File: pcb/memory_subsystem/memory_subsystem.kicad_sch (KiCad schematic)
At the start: 0 parts

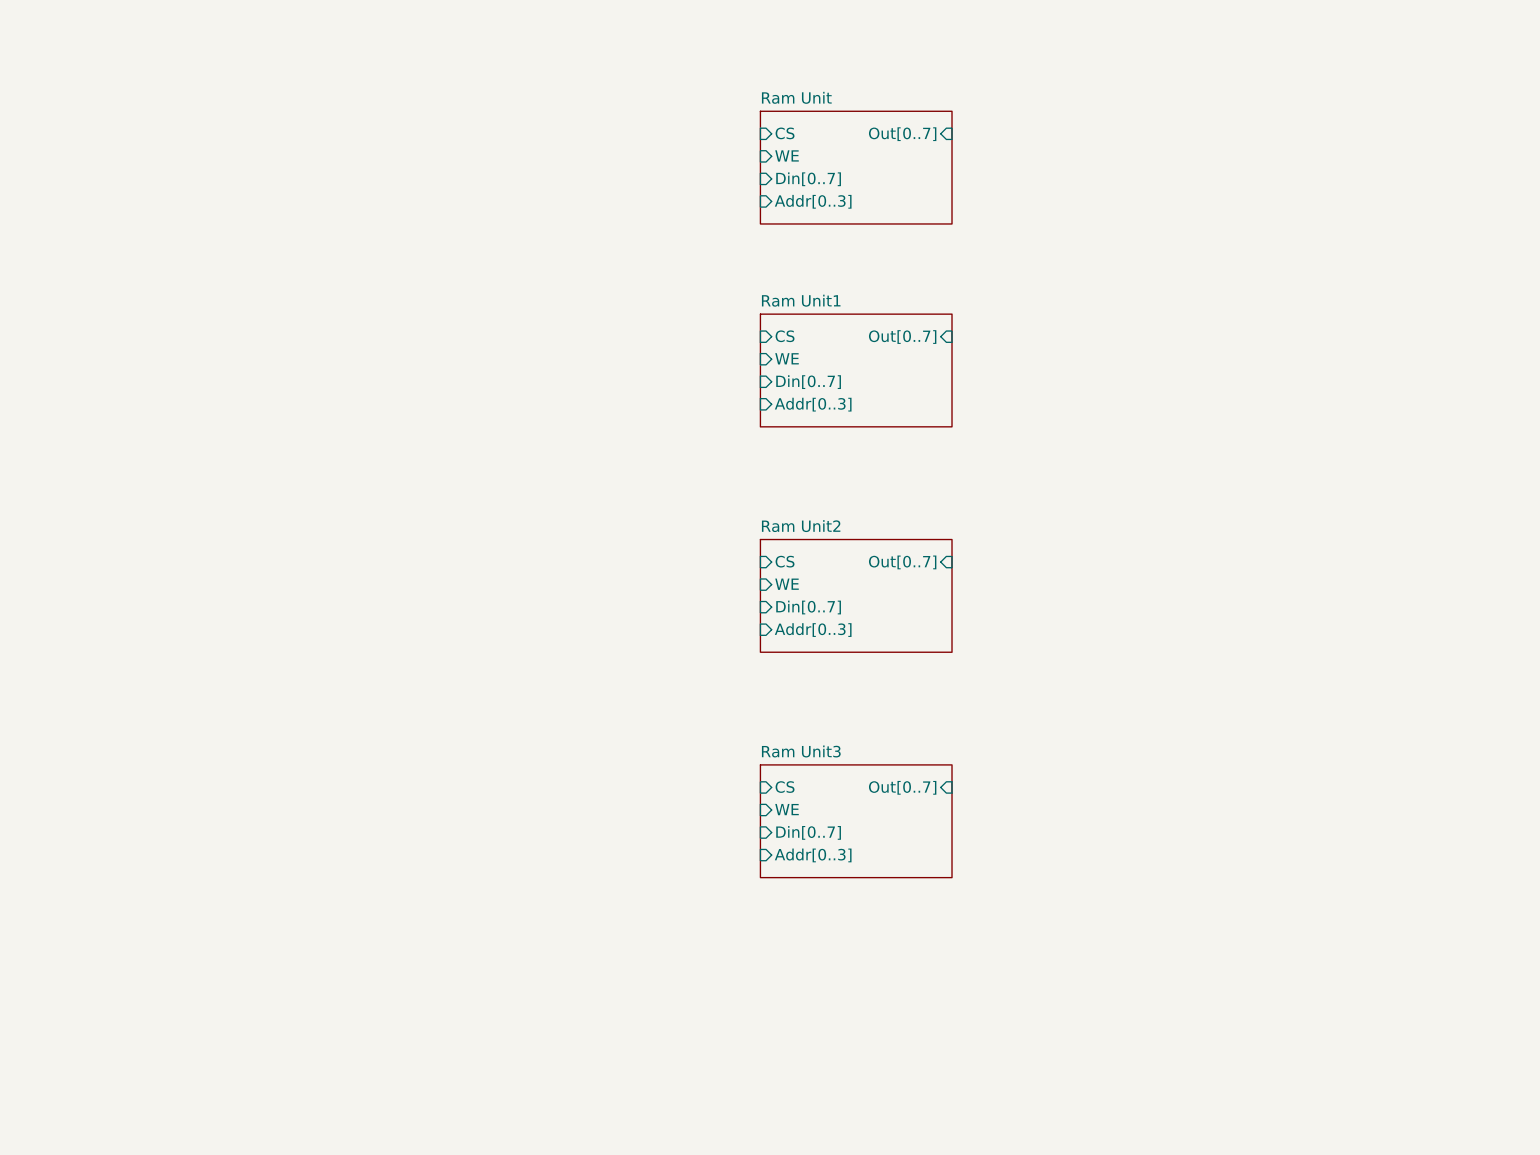
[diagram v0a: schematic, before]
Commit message: Finished first draft of memory subsystem
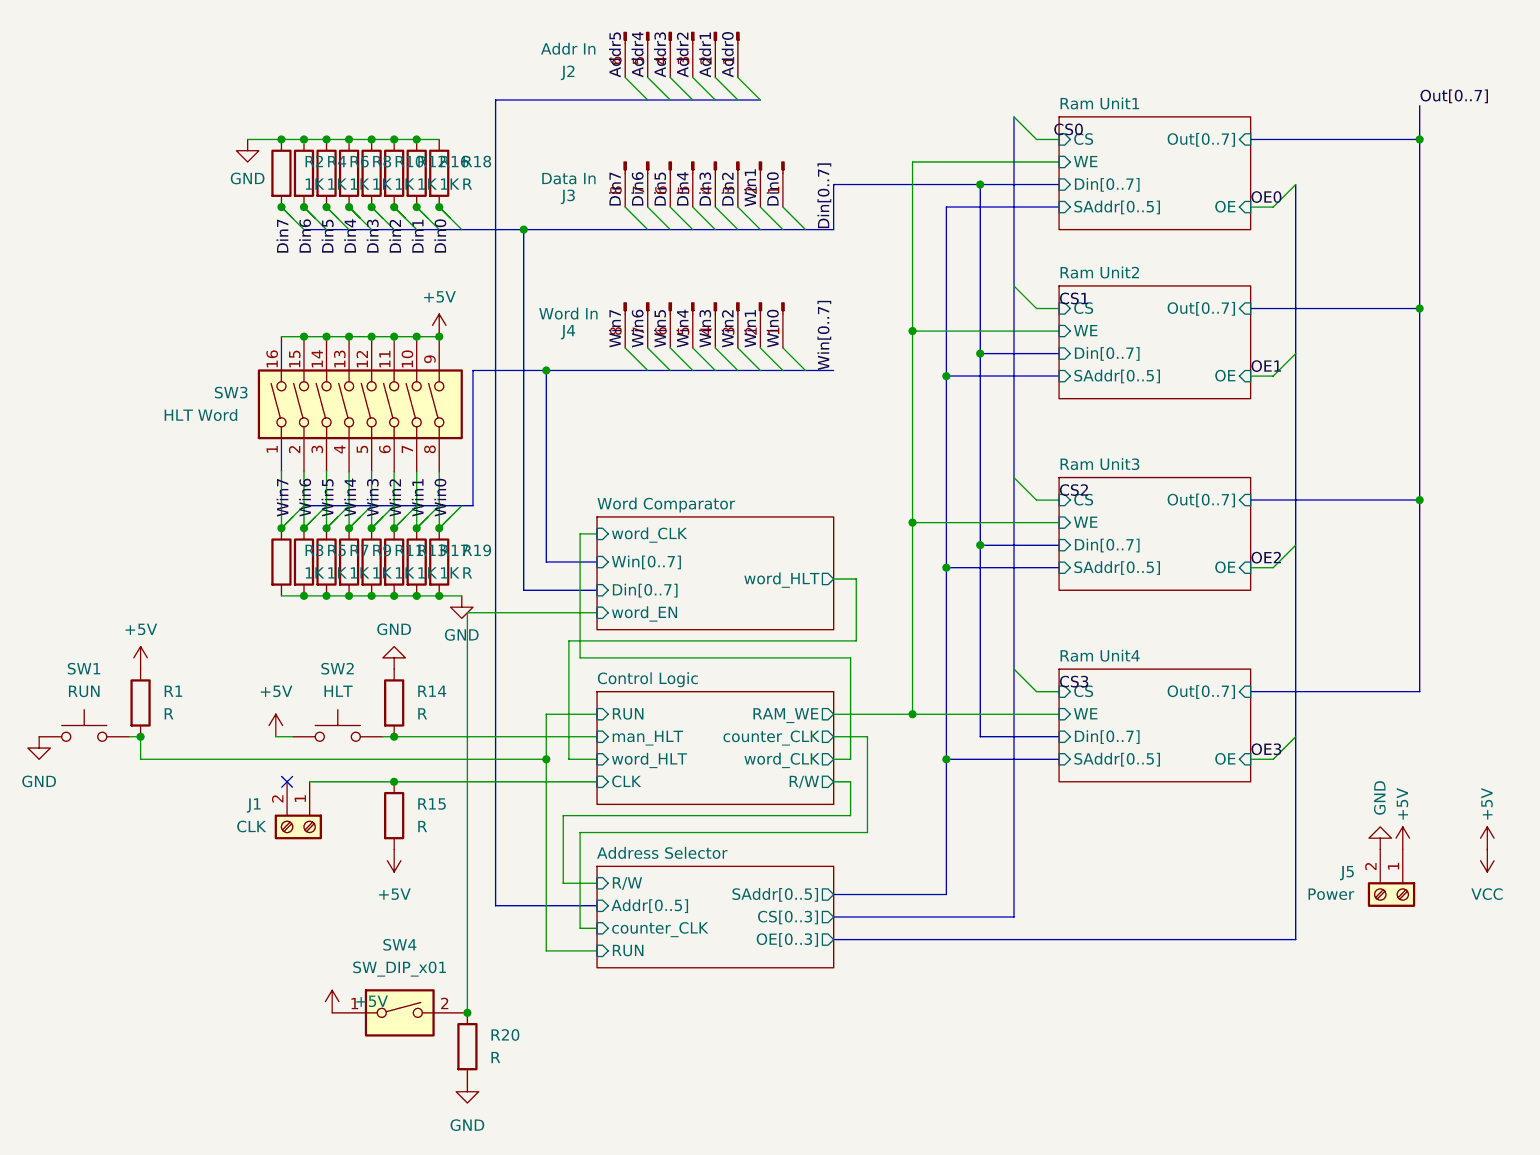
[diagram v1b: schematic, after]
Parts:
- added J1: CLK, symbol Connector:Screw_Terminal_01x02
- added J2: Addr In, symbol Connector:Conn_01x06_Pin
- added J3: Data In, symbol Connector:Conn_01x08_Pin
- added J4: Word In, symbol Connector:Conn_01x08_Pin
- added J5: Power, symbol Connector:Screw_Terminal_01x02
- added R1, R14, R15, R18, R19, R20: R, symbol Device:R
- added R10, R11, R12, R13, R16, R17, R2, R3, R4, R5, R6, R7, R8, R9: 1K, symbol Device:R
- added SW1: RUN, symbol Switch:SW_Push
- added SW2: HLT, symbol Switch:SW_Push
- added SW3: HLT Word, symbol Switch:SW_DIP_x08
- added SW4: SW_DIP_x01, symbol Switch:SW_DIP_x01
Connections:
- new net +5V: J5.1 (Pin_1), R1.1, R15.2, SW2.1, SW3.10, SW3.11, SW3.12, SW3.13, SW3.14, SW3.15, SW3.16, SW3.9, SW4.1
- new net Addr0: J2.1 (Pin_1)
- new net Addr1: J2.2 (Pin_2)
- new net Addr2: J2.3 (Pin_3)
- new net Addr3: J2.4 (Pin_4)
- new net Addr4: J2.5 (Pin_5)
- new net Addr5: J2.6 (Pin_6)
- new net Address Selector/RUN: R1.2, SW1.2
- new net Control Logic/CLK: J1.1 (Pin_1), R15.1
- new net Control Logic/man_HLT: R14.2, SW2.2
- new net Din0: J3.1 (Pin_1), R18.2
- new net Din1: R16.2
- new net Din2: J3.3 (Pin_3), R12.2
- new net Din3: J3.4 (Pin_4), R10.2
- new net Din4: J3.5 (Pin_5), R8.2
- new net Din5: J3.6 (Pin_6), R6.2
- new net Din6: J3.7 (Pin_7), R4.2
- new net Din7: J3.8 (Pin_8), R2.2
- new net GND: J5.2 (Pin_2), R10.1, R11.2, R12.1, R13.2, R14.1, R16.1, R17.2, R18.1, R19.2, R2.1, R20.2, R3.2, R4.1, R5.2, R6.1, R7.2, R8.1, R9.2, SW1.1
- new net Win0: J4.1 (Pin_1), R19.1, SW3.8
- new net Win1: J3.2 (Pin_2), J4.2 (Pin_2), R17.1, SW3.7
- new net Win2: J4.3 (Pin_3), R13.1, SW3.6
- new net Win3: J4.4 (Pin_4), R11.1, SW3.5
- new net Win4: J4.5 (Pin_5), R9.1, SW3.4
- new net Win5: J4.6 (Pin_6), R7.1, SW3.3
- new net Win6: J4.7 (Pin_7), R5.1, SW3.2
- new net Win7: J4.8 (Pin_8), R3.1, SW3.1
- new net Word Comparator/word_EN: R20.1, SW4.2
- no-connect marks 0 -> 1
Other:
- removed sheet Ram Unit
- added sheet Address Selector (address_selector.kicad_sch)
- added sheet Control Logic (control_logic.kicad_sch)
- added sheet Ram Unit4 (RAM_unit.kicad_sch)
- added sheet Word Comparator (word_comparator.kicad_sch)
- sheet Ram Unit1 ports: added OE, SAddr[0..5]; removed Addr[0..3]
- sheet Ram Unit2 ports: added OE, SAddr[0..5]; removed Addr[0..3]
- sheet Ram Unit3 ports: added OE, SAddr[0..5]; removed Addr[0..3]
